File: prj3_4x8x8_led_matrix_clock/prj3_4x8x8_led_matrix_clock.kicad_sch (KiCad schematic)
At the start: 15 parts, among them J1 Barrel_Jack, J2 Conn_01x05_Pin, J3 Conn_01x05_Pin, J4 Conn_01x05_Pin, J5 Conn_01x05_Pin, J6 Conn_01x05_Pin, J7 Conn_01x05_Pin, J8 Conn_01x05_Pin, J9 Conn_01x05_Pin

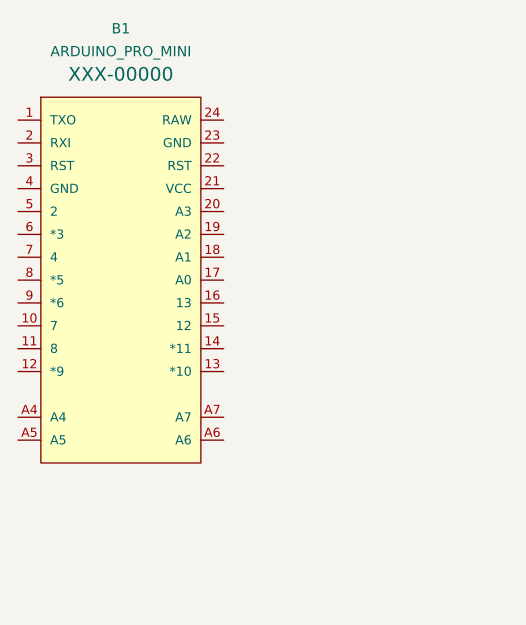
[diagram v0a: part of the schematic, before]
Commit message: Correzione schematico progetto 3
Fix: rimosso simbolo di Arduino Pro Mini perché aveva corrotto lo schema elettrico
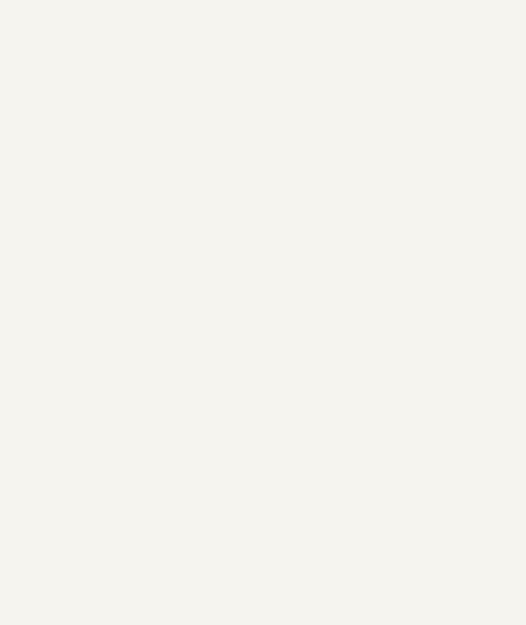
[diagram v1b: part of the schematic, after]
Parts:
- removed B1: ARDUINO_PRO_MINI, ARDUINO_PRO_MINI, symbol SparkFun-Boards:ARDUINO_PRO_MINI
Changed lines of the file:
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@@
-    )
-  )
-  (symbol (lib_id "SparkFun-Boards:ARDUINO_PRO_MINI") (at 66.04 90.17 0) (unit 1)
-    (in_bom yes) (on_board yes) (dnp no) (fields_autoplaced)
-    (property "Reference" "B1" (at 66.04 62.23 0)
-      (effects (font (size 1.143 1.143)))
-    )
-    (property "Value" "ARDUINO_PRO_MINI" (at 66.04 64.77 0)
-      (effects (font (size 1.143 1.143)))
-    )
-    (property "Footprint" "ARDUINO_PRO_MINI" (at 66.04 66.04 0)
-      (effects (font (size 0.508 0.508)) hide)
-    )
-    (property "Datasheet" "" (at 66.04 90.17 0)
-      (effects (font (size 1.27 1.27)) hide)
-    )
-    (property "" "XXX-00000" (at 66.04 67.31 0)
-      (effects (font (size 1.524 1.524)))
-    )
-    (pin "1")
-    (pin "10")
-    (pin "11")
-    (pin "12")
-    (pin "13")
-    (pin "14")
-    (pin "15")
-    (pin "16")
-    (pin "17")
-    (pin "18")
-    (pin "19")
-    (pin "2")
-    (pin "20")
-    (pin "21")
-    (pin "22")
-    (pin "23")
-    (pin "24")
-    (pin "3")
-    (pin "4")
-    (pin "5")
-    (pin "6")
-    (pin "7")
-    (pin "8")
-    (pin "9")
-    (pin "A4")
-    (pin "A5")
-    (pin "A6")
-    (pin "A7")
-    (instances
-      (project "prj3_4x8x8_led_matrix_clock"
-        (path "/361bfe14-206e-4863-a13d-529d9b66dc43"
-          (reference "B1") (unit 1)
-        )
-      )
     )
   )

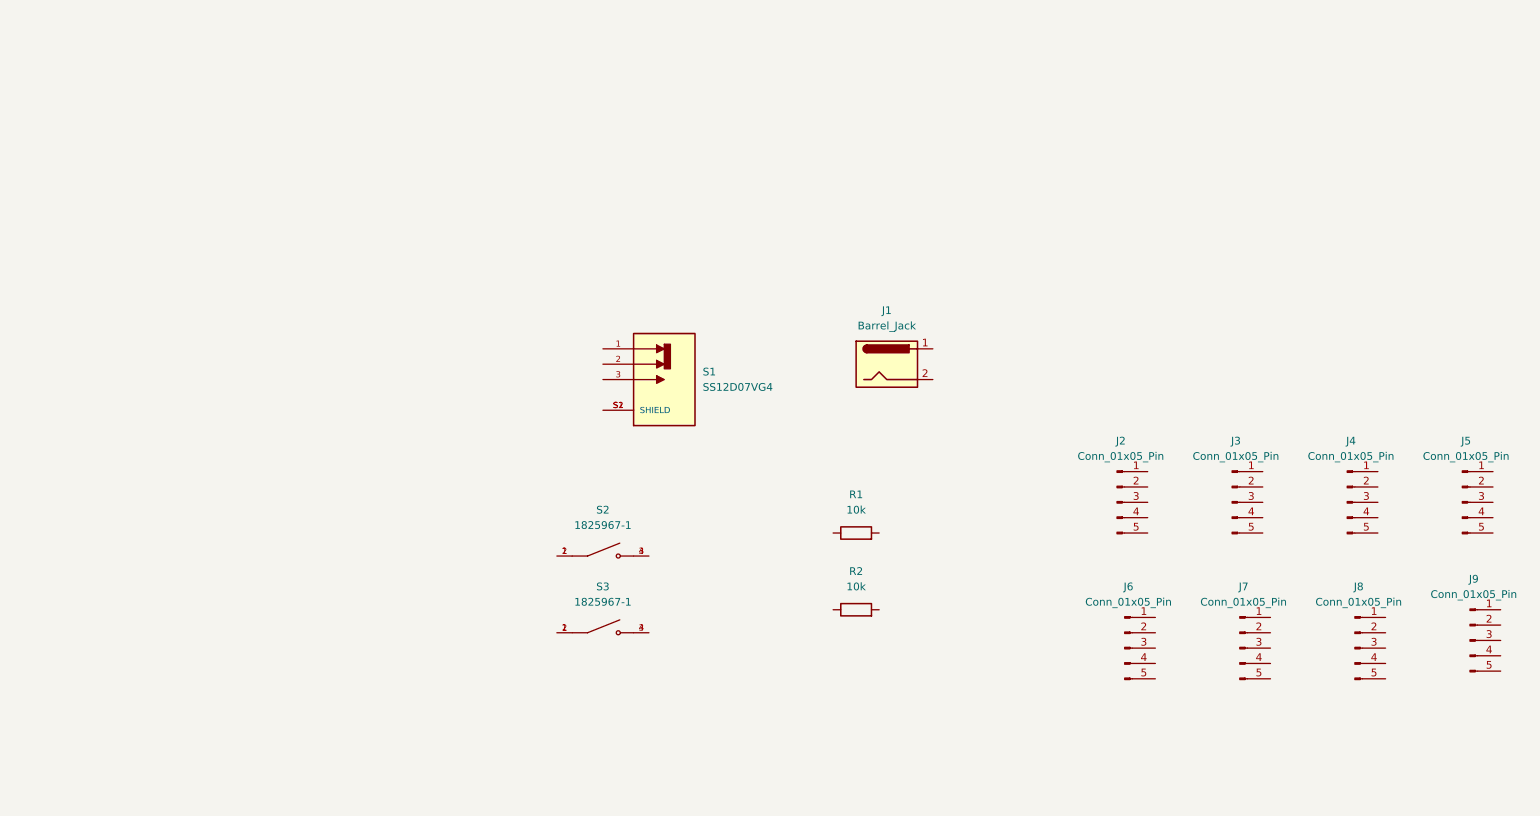
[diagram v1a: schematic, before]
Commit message: Preparati i componenti per le connessioni (no Arduino Pro Mini)
Feat: sistemati i componenti
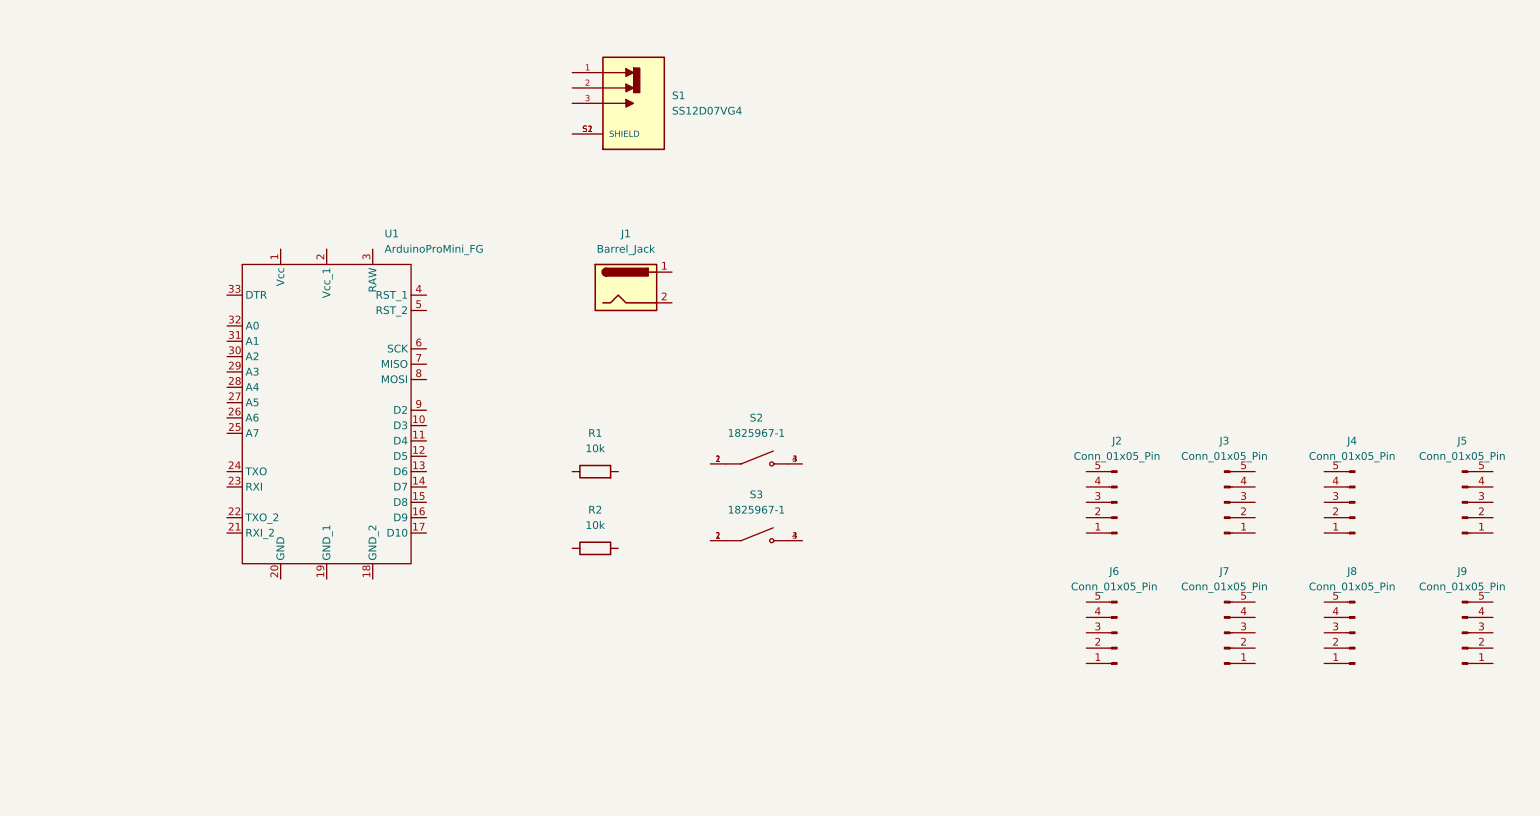
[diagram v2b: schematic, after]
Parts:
- added U1: ArduinoProMini_FG, symbol filippo_arduino_pro_mini:ArduinoProMini_FG
- J1: footprint (none) -> Connector_BarrelJack:BarrelJack_Horizontal
- J2, J3, J4, J5, J6, J7, J8, J9: footprint (none) -> Connector_PinHeader_2.54mm:PinHeader_1x05_P2.54mm_Vertical
- R1, R2: footprint (none) -> Resistor_THT:R_Axial_DIN0204_L3.6mm_D1.6mm_P7.62mm_Horizontal
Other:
- moved on the sheet: J1, J2, J3, J4, J6, J7, J8, J9, R1, R2, S1, S2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

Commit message: Creazione schematico
Feat: create le connessioni tra i componenti dello schema elettrico
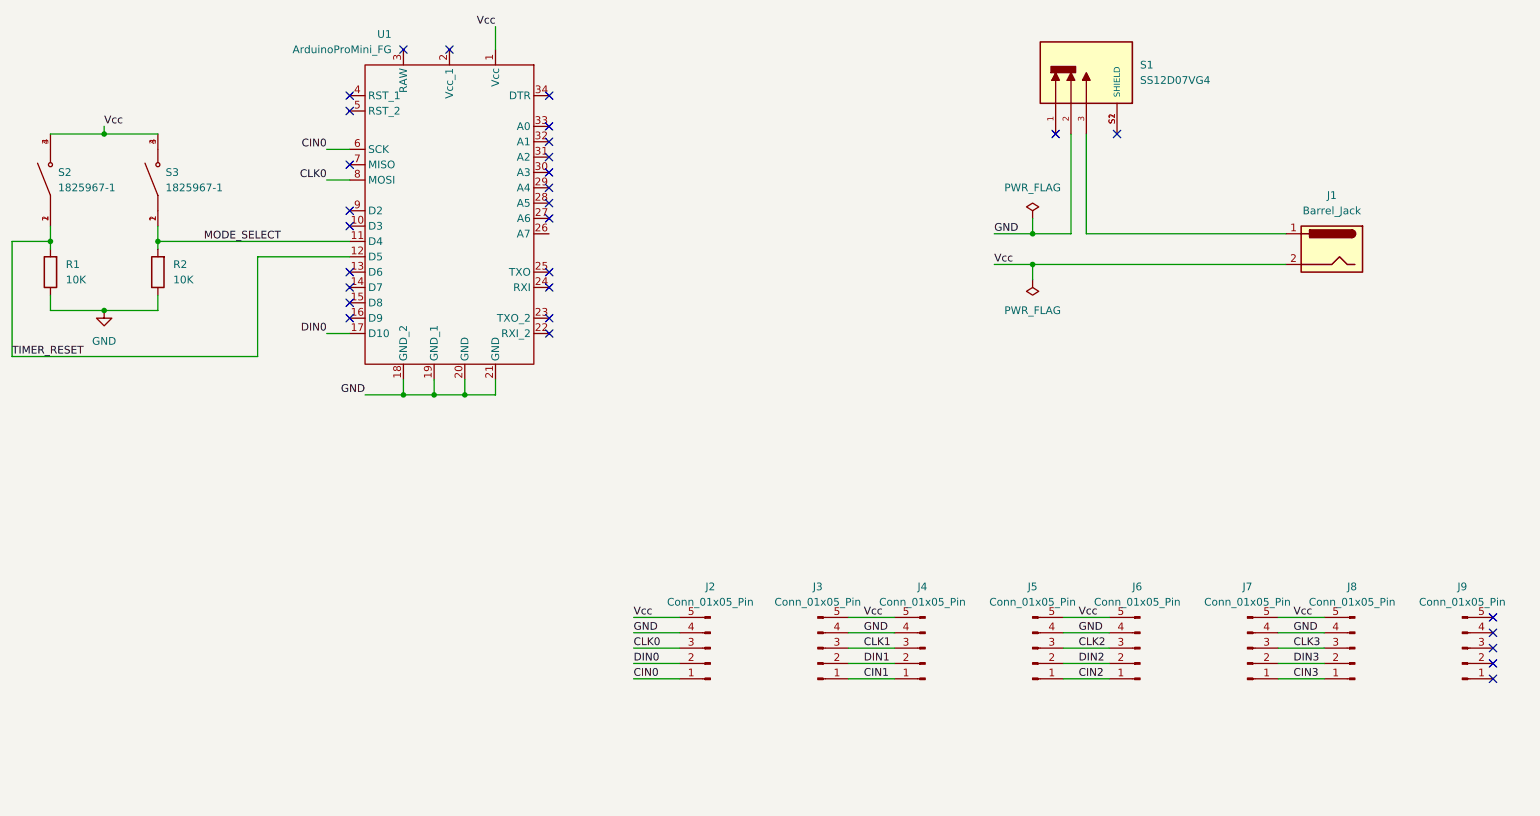
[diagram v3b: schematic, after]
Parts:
- R1, R2: value 10k -> 10K
- U1: footprint (none) -> filippo_arduino_pro_mini:ArduinoProMini_FG
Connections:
- net GND: now reaches R1.1
- net GND: now also J2.4 (Pin_4), J3.4 (Pin_4), J4.4 (Pin_4), J5.4 (Pin_4), J6.4 (Pin_4), J7.4 (Pin_4), J8.4 (Pin_4), R2.1, S1.2, U1.18 (GND_2), U1.19 (GND_1), U1.20 (GND), U1.21 (GND)
- net TIMER_RESET: now reaches R1.2
- net TIMER_RESET: now also S2.1, S2.2, U1.12 (D5)
- net CIN2: now reaches J5.1 (Pin_1)
- net CIN2: now also J6.1 (Pin_1)
- net DIN2: now reaches J5.2 (Pin_2)
- net DIN2: now also J6.2 (Pin_2)
- net CLK2: now reaches J5.3 (Pin_3)
- net CLK2: now also J6.3 (Pin_3)
- net Vcc: now reaches J5.5 (Pin_5)
- net Vcc: now also J1.2, J2.5 (Pin_5), J3.5 (Pin_5), J4.5 (Pin_5), J6.5 (Pin_5), J7.5 (Pin_5), J8.5 (Pin_5), S2.3, S2.4, S3.3, S3.4, U1.1 (Vcc)
- net CIN0: now reaches J2.1 (Pin_1)
- net CIN0: now also U1.6 (SCK)
- net DIN0: now reaches J2.2 (Pin_2)
- net DIN0: now also U1.17 (D10)
- net CLK0: now reaches J2.3 (Pin_3)
- net CLK0: now also U1.8 (MOSI)
- net at J1.1: now also S1.3
- net CIN3: now reaches J8.1 (Pin_1)
- net CIN3: now also J7.1 (Pin_1)
- net DIN3: now reaches J8.2 (Pin_2)
- net DIN3: now also J7.2 (Pin_2)
- net CLK3: now reaches J8.3 (Pin_3)
- net CLK3: now also J7.3 (Pin_3)
- net MODE_SELECT: now reaches U1.11 (D4)
- net MODE_SELECT: now also R2.2, S3.1, S3.2
- net CIN1: now reaches J3.1 (Pin_1)
- net CIN1: now also J4.1 (Pin_1)
- net DIN1: now reaches J3.2 (Pin_2)
- net DIN1: now also J4.2 (Pin_2)
- net CLK1: now reaches J3.3 (Pin_3)
- net CLK1: now also J4.3 (Pin_3)
- no-connect marks 0 -> 30
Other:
- moved on the sheet: J1, J2, J3, J4, J5, J6, J7, J8, J9, R1, R2, S1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

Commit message: Correzioni minori e conclusione schematico progetto 2
Feat: aggiunti mounting hole
Feat: creata grafica
Feat: cambiate alcune diciture
Feat: create net classes
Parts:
- added H1, H2, H3, H4: MountingHole, MountingHole:MountingHole_2.5mm, symbol Mechanical:MountingHole
- J2: value Conn_01x05_Pin -> LED1_IN
- J3: value Conn_01x05_Pin -> LED1_OUT
- J4: value Conn_01x05_Pin -> LED2_IN
- J5: value Conn_01x05_Pin -> LED2_OUT
- J6: value Conn_01x05_Pin -> LED3_IN
- J7: value Conn_01x05_Pin -> LED3_OUT
- J8: value Conn_01x05_Pin -> LED4_IN
- J9: value Conn_01x05_Pin -> LED4_OUT
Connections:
- no-connect marks 30 -> 31
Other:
- note added: "ATT: this connector is flipped vertically so that pin numbers correspond correctly across all headers."

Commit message: Iniziato PCB progetto 3
Feat: impostato PCB
Feat: inserita outline grezza
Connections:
- net Vcc: now also J1.1; no longer J1.2
- net at S1.3: now also J1.2; no longer J1.1
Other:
- moved on the sheet: J1
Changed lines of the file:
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@@
   (junction (at 46.99 62.23) (diameter 0) (color 0 0 0 0)
   )
+  (junction (at 191.77 66.04) (diameter 0) (color 0 0 0 0)
+  )
   (junction (at 38.1 73.66) (diameter 0) (color 0 0 0 0)
   )
@@
   )
   (junction (at 191.77 60.96) (diameter 0) (color 0 0 0 0)
-  )
-  (junction (at 191.77 66.04) (diameter 0) (color 0 0 0 0)
   )
   (junction (at 97.79 87.63) (diameter 0) (color 0 0 0 0)
@@
     (stroke (width 0) (type default))
   )
-  (wire (pts (xy 233.68 60.96) (xy 200.66 60.96))
-    (stroke (width 0) (type default))
-  )
   (wire (pts (xy 38.1 73.66) (xy 29.21 73.66))
     (stroke (width 0) (type default))
@@
   )
   (wire (pts (xy 232.41 132.08) (xy 240.03 132.08))
-    (stroke (width 0) (type default))
-  )
-  (wire (pts (xy 191.77 66.04) (xy 233.68 66.04))
     (stroke (width 0) (type default))
   )
@@
     (stroke (width 0) (type dash_dot))
   )
+  (wire (pts (xy 191.77 66.04) (xy 233.68 66.04))
+    (stroke (width 0) (type default))
+  )
   (wire (pts (xy 63.5 81.28) (xy 63.5 64.77))
     (stroke (width 0) (type default))
@@
   )
   (wire (pts (xy 29.21 44.45) (xy 38.1 44.45))
+    (stroke (width 0) (type default))
+  )
+  (wire (pts (xy 200.66 60.96) (xy 233.68 60.96))
     (stroke (width 0) (type default))
   )
@@
     )
   )
-  (symbol (lib_id "Connector:Barrel_Jack") (at 241.3 63.5 0) (mirror y) (unit 1)
+  (symbol (lib_id "Connector:Barrel_Jack") (at 241.3 63.5 180) (unit 1)
     (in_bom yes) (on_board yes) (dnp no)
-    (property "Reference" "J1" (at 241.3 54.61 0)
-      (effects (font (size 1.27 1.27)))
-    )
-    (property "Value" "Barrel_Jack" (at 241.3 57.15 0)
-      (effects (font (size 1.27 1.27)))
-    )
-    (property "Footprint" "Connector_BarrelJack:BarrelJack_Horizontal" (at 240.03 64.516 0)
-      (effects (font (size 1.27 1.27)) hide)
-    )
-    (property "Datasheet" "~" (at 240.03 64.516 0)
-      (effects (font (size 1.27 1.27)) hide)
-    )
+    (property "Reference" "J1" (at 241.3 72.39 0)
+      (effects (font (size 1.27 1.27)))
+    )
+    (property "Value" "Barrel_Jack" (at 241.3 69.85 0)
+      (effects (font (size 1.27 1.27)))
+    )
+    (property "Footprint" "Connector_BarrelJack:BarrelJack_Horizontal" (at 240.03 62.484 0)
+      (effects (font (size 1.27 1.27)) hide)
+    )
+    (property "Datasheet" "~" (at 240.03 62.484 0)
+      (effects (font (size 1.27 1.27)) hide)
+    )

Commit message: Ultimi ritocchi progetto 3 e correzioni
Feat: aggiunte/aggiustate varie silkscreen
Feat: aggiunti modelli 3D mancanti
Fix: corretti nomi dei net nello schematico e nel PCB
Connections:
- net CIN0 is gone; now on net CLK0: J2.1 (Pin_1), U1.6 (SCK)
- net CIN1 is gone; now on net CLK1: J3.1 (Pin_1), J4.1 (Pin_1)
- net CIN2 is gone; now on net CLK2: J5.1 (Pin_1), J6.1 (Pin_1)
- net CIN3 is gone; now on net CLK3: J7.1 (Pin_1), J8.1 (Pin_1)
- net CLK0: no longer J2.3 (Pin_3), U1.8 (MOSI)
- net CLK1: no longer J3.3 (Pin_3), J4.3 (Pin_3)
- net CLK2: no longer J5.3 (Pin_3), J6.3 (Pin_3)
- net CLK3: no longer J7.3 (Pin_3), J8.3 (Pin_3)
- net DIN0: now also J2.3 (Pin_3), U1.8 (MOSI); no longer J2.2 (Pin_2), U1.17 (D10)
- net DIN1: now also J3.3 (Pin_3), J4.3 (Pin_3); no longer J3.2 (Pin_2), J4.2 (Pin_2)
- net DIN2: now also J5.3 (Pin_3), J6.3 (Pin_3); no longer J5.2 (Pin_2), J6.2 (Pin_2)
- net DIN3: now also J7.3 (Pin_3), J8.3 (Pin_3); no longer J7.2 (Pin_2), J8.2 (Pin_2)
- new net CS0: J2.2 (Pin_2), U1.17 (D10)
- new net CS1: J3.2 (Pin_2), J4.2 (Pin_2)
- new net CS2: J5.2 (Pin_2), J6.2 (Pin_2)
- new net CS3: J7.2 (Pin_2), J8.2 (Pin_2)
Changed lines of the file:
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@@
     (effects (font (size 1.27 1.27)) (justify left bottom))
   )
-  (label "CLK0" (at 125.73 129.54 0) (fields_autoplaced)
+  (label "CLK0" (at 125.73 134.62 0) (fields_autoplaced)
     (effects (font (size 1.27 1.27)) (justify left bottom))
   )
-  (label "CIN3" (at 234.95 134.62 0) (fields_autoplaced)
+  (label "CS3" (at 234.95 132.08 0) (fields_autoplaced)
     (effects (font (size 1.27 1.27)) (justify left bottom))
   )
-  (label "CLK2" (at 199.39 129.54 0) (fields_autoplaced)
+  (label "CLK2" (at 199.39 134.62 0) (fields_autoplaced)
     (effects (font (size 1.27 1.27)) (justify left bottom))
   )
-  (label "CLK0" (at 74.93 52.07 180) (fields_autoplaced)
+  (label "CLK0" (at 74.93 46.99 180) (fields_autoplaced)
     (effects (font (size 1.27 1.27)) (justify right bottom))
   )
-  (label "DIN1" (at 163.83 132.08 0) (fields_autoplaced)
+  (label "DIN1" (at 163.83 129.54 0) (fields_autoplaced)
     (effects (font (size 1.27 1.27)) (justify left bottom))
   )
-  (label "CLK1" (at 163.83 129.54 0) (fields_autoplaced)
+  (label "CLK1" (at 163.83 134.62 0) (fields_autoplaced)
     (effects (font (size 1.27 1.27)) (justify left bottom))
   )
@@
     (effects (font (size 1.27 1.27)) (justify left bottom))
   )
-  (label "DIN2" (at 199.39 132.08 0) (fields_autoplaced)
+  (label "DIN2" (at 199.39 129.54 0) (fields_autoplaced)
     (effects (font (size 1.27 1.27)) (justify left bottom))
   )
-  (label "CIN0" (at 125.73 134.62 0) (fields_autoplaced)
+  (label "CS0" (at 125.73 132.08 0) (fields_autoplaced)
     (effects (font (size 1.27 1.27)) (justify left bottom))
   )
@@
     (effects (font (size 1.27 1.27)) (justify left bottom))
   )
-  (label "CIN2" (at 199.39 134.62 0) (fields_autoplaced)
+  (label "CS2" (at 199.39 132.08 0) (fields_autoplaced)
     (effects (font (size 1.27 1.27)) (justify left bottom))
   )
@@
     (effects (font (size 1.27 1.27)) (justify left bottom))
   )
-  (label "CIN1" (at 163.83 134.62 0) (fields_autoplaced)
+  (label "CS1" (at 163.83 132.08 0) (fields_autoplaced)
     (effects (font (size 1.27 1.27)) (justify left bottom))
   )
-  (label "DIN0" (at 125.73 132.08 0) (fields_autoplaced)
+  (label "DIN0" (at 125.73 129.54 0) (fields_autoplaced)
     (effects (font (size 1.27 1.27)) (justify left bottom))
   )
-  (label "DIN0" (at 74.93 77.47 180) (fields_autoplaced)
+  (label "DIN0" (at 74.93 52.07 180) (fields_autoplaced)
     (effects (font (size 1.27 1.27)) (justify right bottom))
   )
-  (label "DIN3" (at 234.95 132.08 0) (fields_autoplaced)
+  (label "DIN3" (at 234.95 129.54 0) (fields_autoplaced)
     (effects (font (size 1.27 1.27)) (justify left bottom))
   )
-  (label "CIN0" (at 74.93 46.99 180) (fields_autoplaced)
+  (label "CS0" (at 74.93 77.47 180) (fields_autoplaced)
     (effects (font (size 1.27 1.27)) (justify right bottom))
   )
-  (label "CLK3" (at 234.95 129.54 0) (fields_autoplaced)
+  (label "CLK3" (at 234.95 134.62 0) (fields_autoplaced)
     (effects (font (size 1.27 1.27)) (justify left bottom))
   )
